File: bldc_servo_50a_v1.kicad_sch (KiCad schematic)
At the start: 79 parts

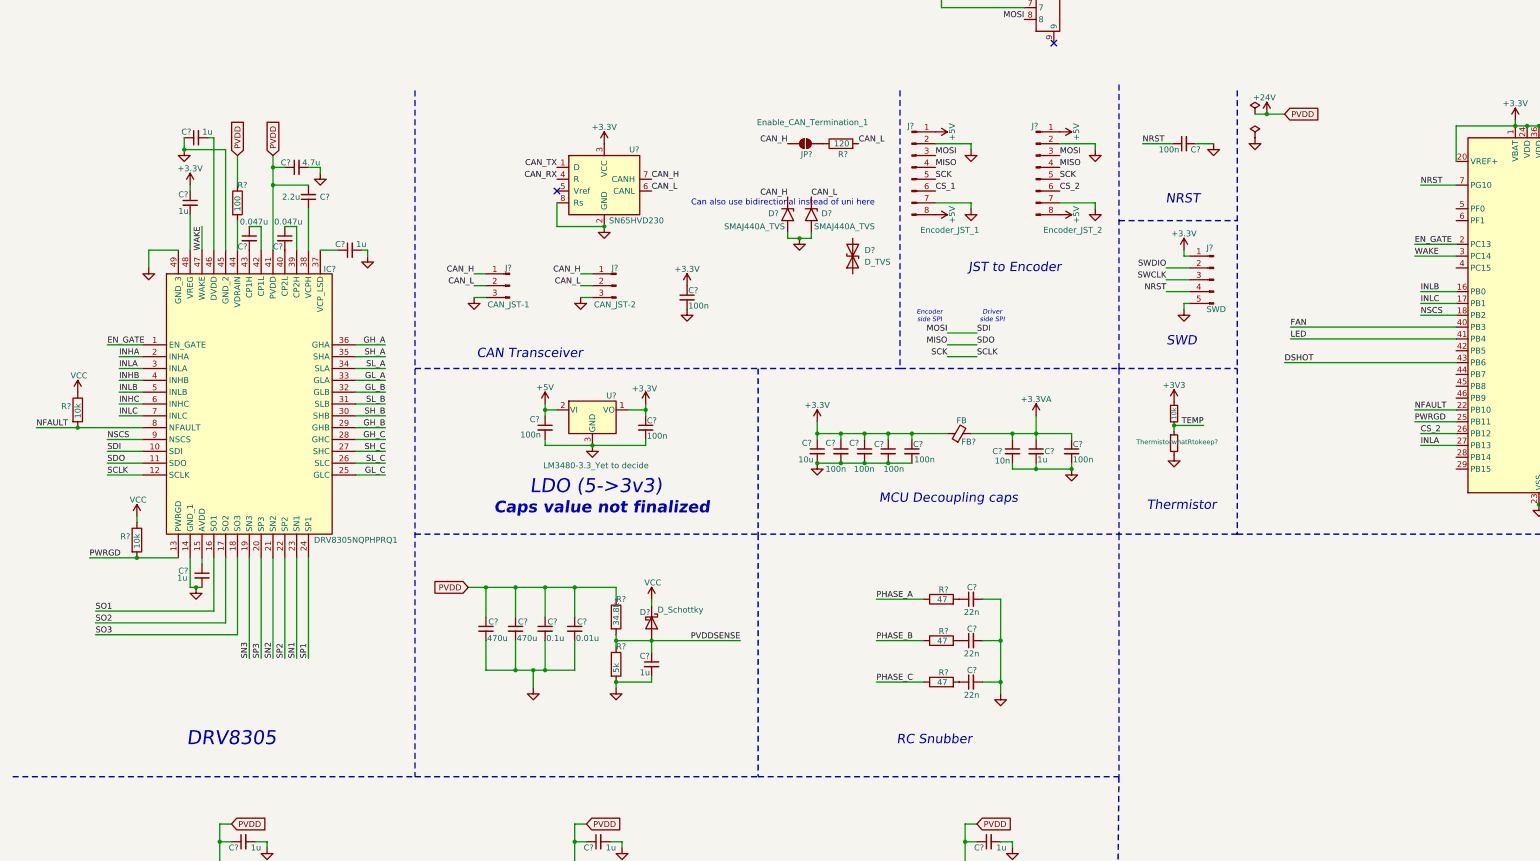
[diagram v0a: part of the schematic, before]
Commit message: Added FAN JST
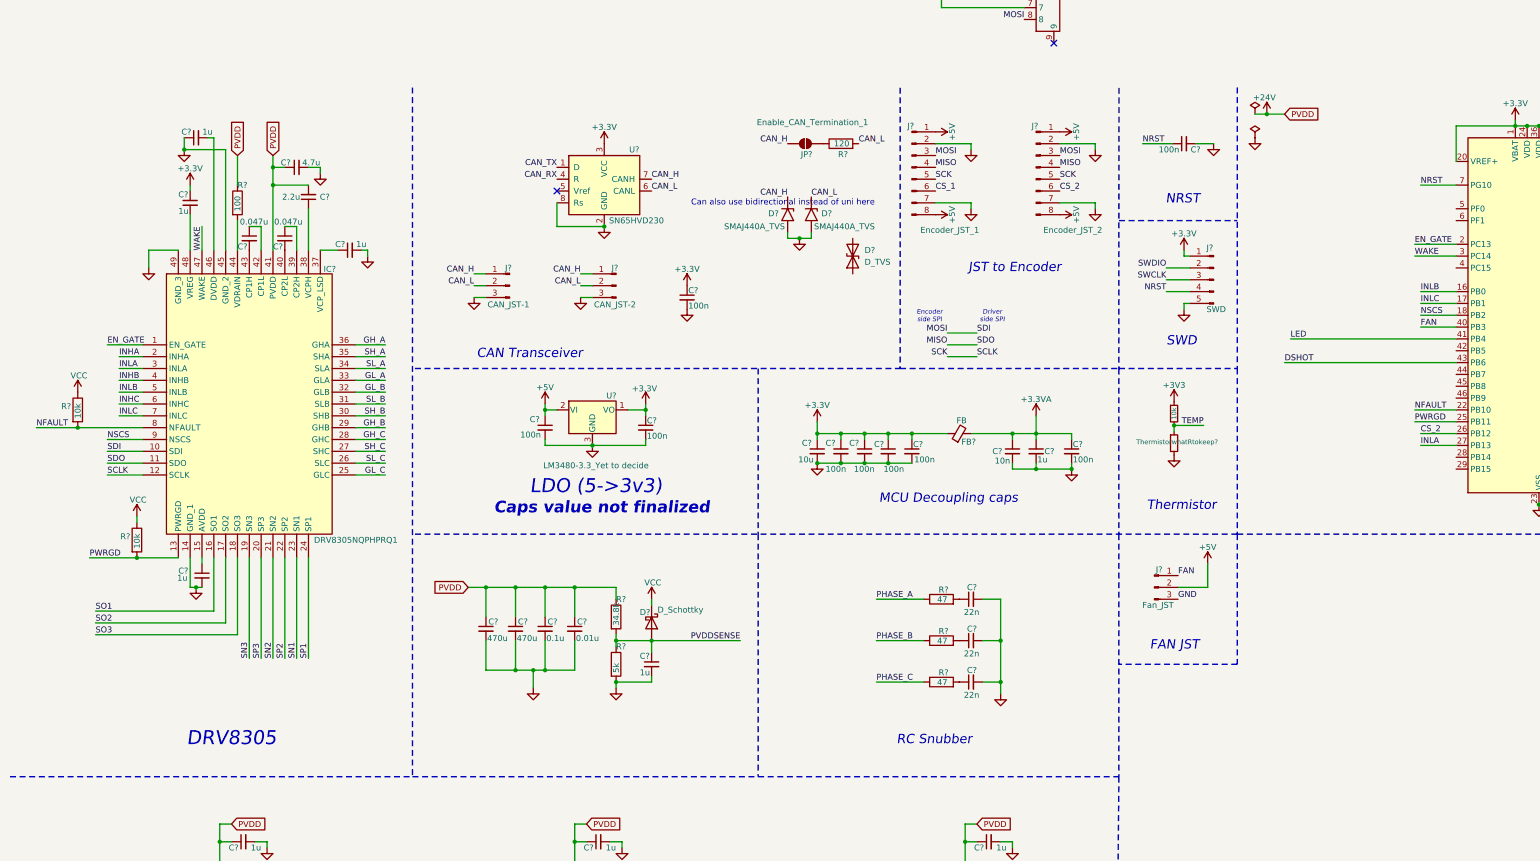
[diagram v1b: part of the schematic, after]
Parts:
- added J?: Fan_JST, Connector_JST:JST_EH_B3B-EH-A_1x03_P2.50mm_Vertical, symbol Connector:Conn_01x03_Pin
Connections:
- net +5V: now also J?.2 (Pin_2)
- net FAN: now also J?.1 (Pin_1)
- net GND: now also J?.3 (Pin_3)
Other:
- note added: "FAN JST"
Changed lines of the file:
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@@
 		)
 	)
+	(text "FAN JST"
+		(exclude_from_sim no)
+		(at 262.128 131.826 0)
+		(effects
+			(font
+				(size 2 2)
+				(thickness 0.375)
+				(italic yes)
+			)
+		)
+	)
 	(text "MCU Decoupling caps\n"
 		(exclude_from_sim no)
@@
 	(polyline
 		(pts
-			(xy 99.06 12.7) (xy 99.06 160.02)
+			(xy 98.523 12.0658) (xy 98.523 160.02)
 		)
 		(stroke
@@
 	(polyline
 		(pts
-			(xy 99.06 160.02) (xy 172.72 160.02)
+			(xy 98.523 160.02) (xy 172.72 160.02)
 		)
 		(stroke
@@
 	(polyline
 		(pts
-			(xy 275.59 12.7) (xy 275.59 72.39)
+			(xy 275.5966 12.0572) (xy 275.59 72.39)
 		)
 		(stroke
@@
 	(polyline
 		(pts
-			(xy 203.2 12.7) (xy 203.2 72.39)
+			(xy 203.2139 12.1194) (xy 203.2 72.39)
 		)
 		(stroke
@@
 	(wire
 		(pts
+			(xy 269.24 119.38) (xy 262.89 119.38)
+		)
+		(stroke
+			(width 0)
+			(type default)
+		)
+	)
+	(wire
+		(pts
 			(xy 133.35 130.81) (xy 133.35 137.16)
 		)
@@
 	(polyline
 		(pts
-			(xy 12.7 160.02) (xy 99.06 160.02)
+			(xy 12.1278 160.02) (xy 98.523 160.02)
 		)
 		(stroke
@@
 	(wire
 		(pts
-			(xy 287.02 63.5) (xy 322.58 63.5)
+			(xy 314.96 63.5) (xy 322.58 63.5)
 		)
 		(stroke
@@
 	(wire
 		(pts
+			(xy 269.24 114.3) (xy 269.24 119.38)
+		)
+		(stroke
+			(width 0)
+			(type default)
+		)
+	)
+	(wire
+		(pts
 			(xy 213.36 215.9) (xy 213.36 218.44)
 		)
@@
 		)
 	)
+	(polyline
+		(pts
+			(xy 275.59 107.95) (xy 275.59 135.89)
+		)
+		(stroke
+			(width 0.3)
+			(type dash)
+		)
+	)
 	(wire
 		(pts
@@
 	(polyline
 		(pts
-			(xy 250.19 11.43) (xy 250.19 72.39)
+			(xy 250.1945 12.1485) (xy 250.19 72.39)
 		)
 		(stroke
@@
 		)
 	)
+	(polyline
+		(pts
+			(xy 275.59 135.89) (xy 250.19 135.89)
+		)
+		(stroke
+			(width 0.3)
+			(type dash)
+		)
+	)
 	(wire
 		(pts
@@
 		)
 	)
+	(label "FAN"
+		(at 262.89 116.84 0)
+		(effects
+			(font
+				(size 1.27 1.27)
+			)
+			(justify left bottom)
+		)
+	)
 	(label "NRST"
 		(at 314.96 33.02 0)
@@
 	)
 	(label "FAN"
-		(at 287.02 63.5 0)
+		(at 314.96 63.5 0)
 		(effects
 			(font
@@
 		)
 	)
+	(label "GND"
+		(at 262.89 121.92 0)
+		(effects
+			(font
+				(size 1.27 1.27)
+			)
+			(justify left bottom)
+		)
+	)
 	(label "SH_A"
 		(at 92.71 69.85 180)
@@
 	)
 	(symbol
+		(lib_id "Connector:Conn_01x03_Pin")
+		(at 257.81 119.38 0)
+		(unit 1)
+		(exclude_from_sim no)
+		(in_bom yes)
+		(on_board yes)
+		(dnp no)
+		(property "Reference" "J?"
+			(at 258.826 115.57 0)
+			(effects
+				(font
+					(size 1.27 1.27)
+				)
+			)
+		)
+		(property "Value" "Fan_JST"
+			(at 258.572 123.19 0)
+			(effects
+				(font
+					(size 1.27 1.27)
+				)
+			)
+		)
+		(property "Footprint" "Connector_JST:JST_EH_B3B-EH-A_1x03_P2.50mm_Vertical"
+			(at 257.81 119.38 0)
+			(effects
+				(font
+					(size 1.27 1.27)
+				)
+				(hide yes)
+			)
+		)
+		(property "Datasheet" "~"
+			(at 257.81 119.38 0)
+			(effects
+				(font
+					(size 1.27 1.27)
+				)
+				(hide yes)
+			)
+		)
+		(property "Description" "Generic connector, single row, 01x03, script generated"
+			(at 257.81 119.38 0)
+			(effects
+				(font
+					(size 1.27 1.27)
+				)
+				(hide yes)
+			)
+		)
+		(pin "1"
+		)
+		(pin "2"
+		)
+		(pin "3"
+		)
+		(instances
+			(project ""
+				(path "/ca0f1187-2401-4955-9ff2-f596d64fa8e9"
+					(reference "J?")
+					(unit 1)
+				)
+			)
+		)
+	)
+	(symbol
 		(lib_id "Connector:Conn_01x08_Pin")
 		(at 205.74 29.21 0)
@@
 					(unit 1)
 				)
+			)
+		)
+	)
+	(symbol
+		(lib_id "power:+5V")
+		(at 269.24 114.3 0)
+		(unit 1)
+		(exclude_from_sim no)
+		(in_bom yes)
+		(on_board yes)
+		(dnp no)
+		(property "Reference" "#PWR017"
+			(at 269.24 118.11 0)
+			(effects
+				(font
+					(size 1.27 1.27)
+				)
+				(hide yes)
+			)
+		)
+		(property "Value" "+5V"
+			(at 269.24 110.744 0)
+			(effects
+				(font
+					(size 1.27 1.27)
+				)
+			)
+		)
+		(property "Footprint" ""
+			(at 269.24 114.3 0)
+			(effects
+				(font
+					(size 1.27 1.27)
+				)
+				(hide yes)
+			)
+		)
+		(property "Datasheet" ""
+			(at 269.24 114.3 0)
+			(effects
+				(font
+					(size 1.27 1.27)
+				)
+				(hide yes)
+			)
+		)
+		(property "Description" "Power symbol creates a global label with name \"+5V\""
+			(at 269.24 114.3 0)
+			(effects
+				(font
+					(size 1.27 1.27)
+				)
+				(hide yes)
+			)
+		)
+		(pin "1"
+		)
+		(instances
+			(project "bldc_servo_50a_v1"
+				(path "/ca0f1187-2401-4955-9ff2-f596d64fa8e9"
+					(reference "#PWR017")
+					(unit 1)
+				)

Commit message: Added FAN JST
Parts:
- removed D?: D_TVS, symbol Device:D_TVS
- removed FPC1: External_sensor, HCTL HC-FPC-05-09-8RLTAG:FPC-SMD_8P-P0.50_HC-FPC-05-09-8RLTAG, symbol HCTL HC-FPC-05-09-8RLTAG:HC-FPC-05-09-8RLTAG
- added FPC1, FPC2: External sensor, HCTL HC-FPC-05-09-8RLTAG_8pin connector:FPC-SMD_8P-P0.50_HC-FPC-05-09-8RLTAG, symbol HCTL HC-FPC-05-09-8RLTAG_8pin connector:HC-FPC-05-09-8RLTAG
- added R19, R21, R23: 34.8k, symbol Device:R
- added R20, R22, R24: 5k, symbol Device:R
- added SW?: SW_SPDT, symbol Switch:SW_SPDT
- 10k1: renamed from 10k; footprint (none) -> Resistor_SMD:R_0402_1005Metric_Pad0.72x0.64mm_HandSolder
- C1: renamed from C?; footprint (none) -> Capacitor_SMD:C_0402_1005Metric_Pad0.74x0.62mm_HandSolder; partno (none) -> C6119811
- C2, C3, C4: renamed from C?; footprint (none) -> Capacitor_SMD:C_0402_1005Metric_Pad0.74x0.62mm_HandSolder
- gave numbers to parts that had none: 73
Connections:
- net VCC is gone; now on net +3.3V: D2.1 (K), R1.1, R2.1
- net +3.3V: now also FPC1.2, FPC1.7, FPC2.2, FPC2.7
- net +5V: now also SW?.1 (A); no longer J5.2 (Pin_2)
- net CS_1: now also FPC1.6
- net CS_2: now also U3.39 (PA15), FPC2.6; no longer U3.26 (PB12)
- net FAN: now also U3.41 (PB4); no longer U3.40 (PB3)
- net GND: now also FPC1.4, FPC1.5, FPC2.4, FPC2.5, R20.2, R22.2, R24.2, SW?.3 (C)
- net INLB: now also U3.28 (PB14); no longer U3.16 (PB0)
- net INLC: now also U3.29 (PB15); no longer U3.17 (PB1)
- net LED: now also U3.42 (PB5); no longer U3.41 (PB4)
- net MISO: now also FPC1.1, FPC2.1
- net MOSI: now also FPC1.8, FPC2.8
- net NSCS: no longer U3.18 (PB2)
- net PHASE_A: now also R19.1
- net PHASE_B: now also R21.1
- net PHASE_C: now also R23.1
- net PVDDSENSE: now also U3.6 (PF1)
- net SCK: now also FPC1.3, FPC2.3
- net TEMP: now also U3.18 (PB2); no longer U3.11 (PA3)
- net SH_B_SENSE: now reaches U3.5 (PF0)
- net SH_B_SENSE: now also R21.2, R22.1
- net DSHOT: no longer names the net of U3.43 (PB6)
- new net FAN_SW: J5.2 (Pin_2), SW?.2 (B)
- new net SH_A_SENSE: R19.2, R20.1, U3.11 (PA3)
- new net SH_C_SENSE: R23.2, R24.1, U3.17 (PB1)
- no-connect marks 3 -> 5
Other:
- note added: "Encoder Connectors"
- note added: "FAN Switch"
- note added: "Phase Voltage Sensing"
- note added: "short with any GPIO"

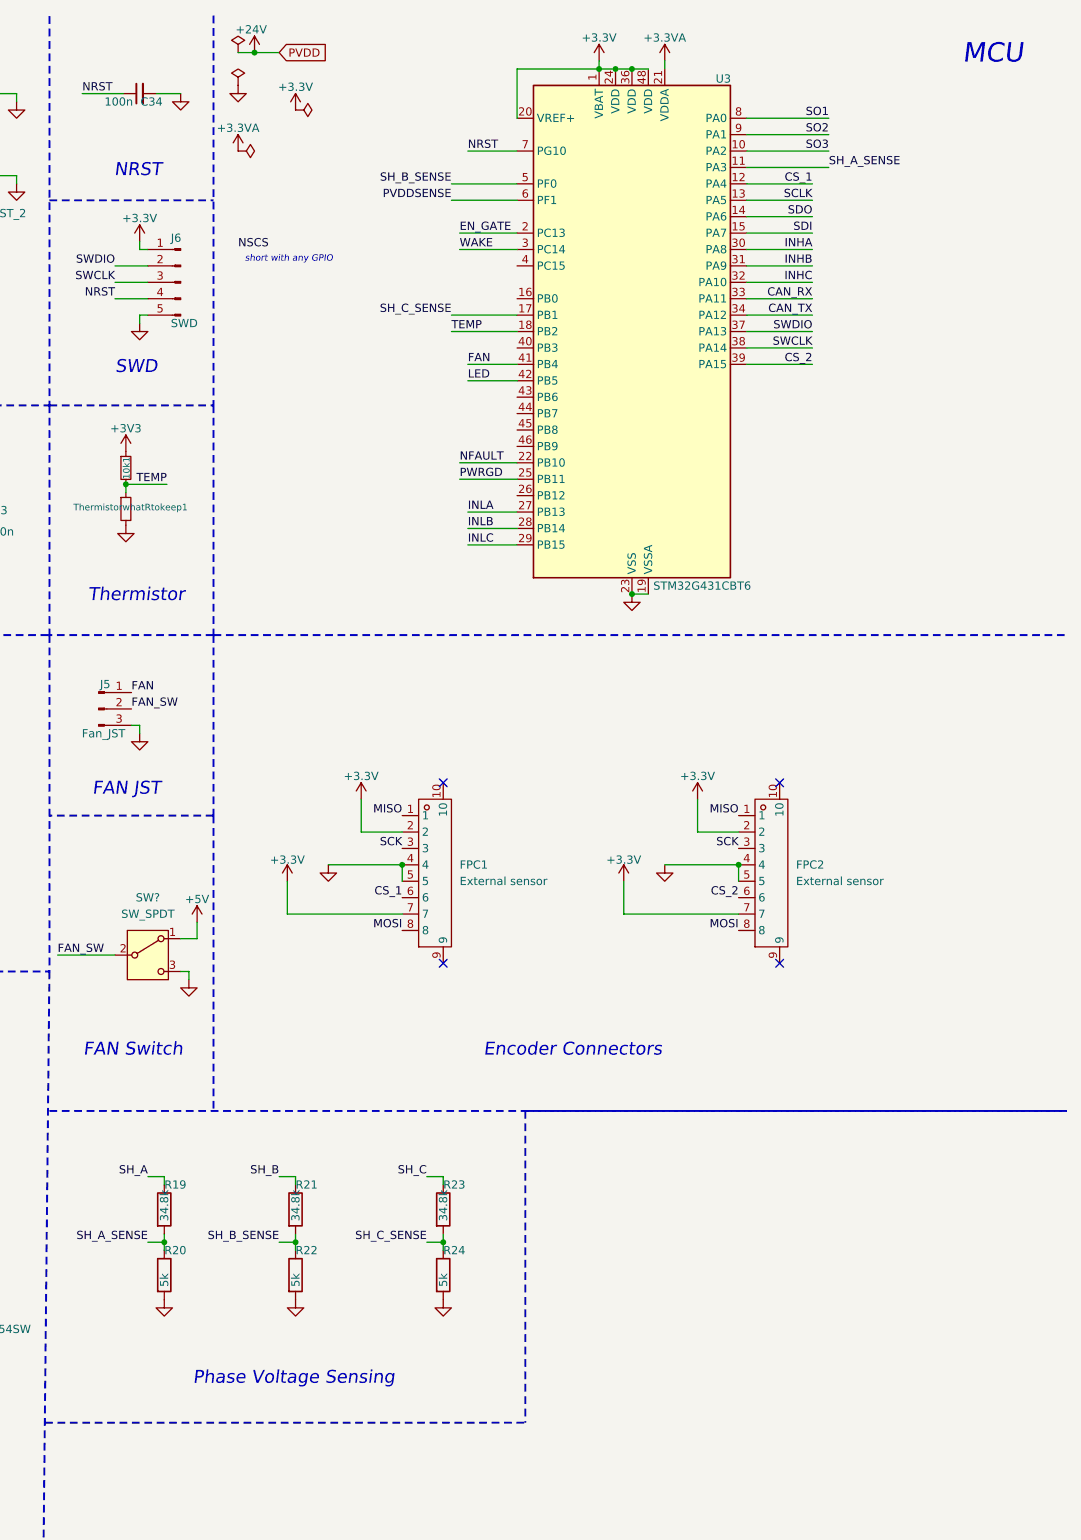
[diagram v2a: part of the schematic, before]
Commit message: Completed full schematic. No ERC errors. Need to be reviewed once.
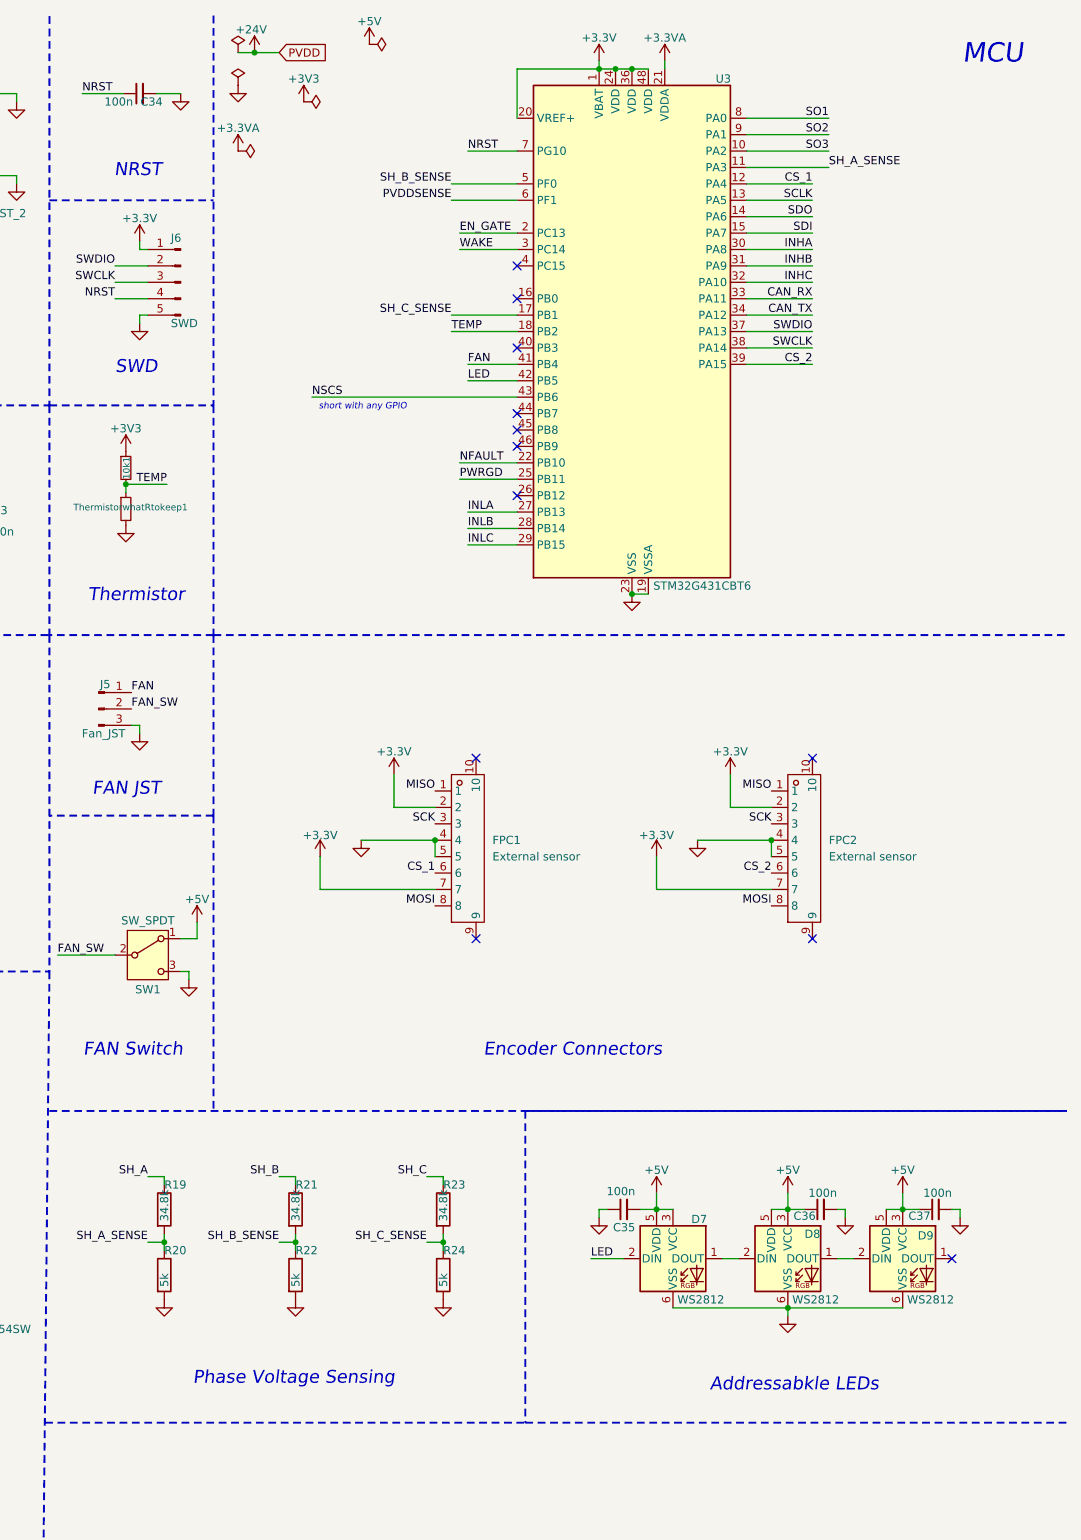
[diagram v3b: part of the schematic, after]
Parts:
- added C35, C36, C37: 100n, symbol Device:C_Small
- added D7, D8, D9: WS2812, LED_SMD:LED_WS2812_PLCC6_5.0x5.0mm_P1.6mm, symbol LED:WS2812
- gave numbers to parts that had none: 1
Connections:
- net +5V: now also C35.2, C36.1, C37.1, D7.3 (VCC), D7.5 (VDD), D8.3 (VCC), D8.5 (VDD), D9.3 (VCC), D9.5 (VDD)
- net GND: now also C35.1, C36.2, C37.2, D7.6 (VSS), D8.6 (VSS), D9.6 (VSS)
- net LED: now also D7.2 (DIN)
- net NSCS: now also U3.43 (PB6)
- new net: D7.1 (DOUT), D8.2 (DIN)
- new net: D8.1 (DOUT), D9.2 (DIN)
- no-connect marks 5 -> 13
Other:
- note added: "Addressabkle LEDs"
- moved on the sheet: FPC1, FPC2
